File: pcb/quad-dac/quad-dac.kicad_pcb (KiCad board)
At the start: 2 copper layers, 90 x 90 mm, 18 parts, among them J1 Power+SPI, J2 CV_OUT, U1 AD5754R

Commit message: pcbs
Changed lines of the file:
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@@
   ;; =========================================================================
   ;; ── U1: AD5754R — TSSOP-24 ────────────────────────────────────────────
+  ;; Pin mapping: AD5754R pin 1 (AVSS) at top-left → KiCad pad 1 at (-2.8625, 3.575)
+  ;; Counter-clockwise: pads 1-12 left side (top→bottom), pads 13-24 right side (bottom→top)
   (footprint "Package_SO:TSSOP-24_4.4x7.8mm_P0.65mm"
     (layer "F.Cu")
@@
     (property "Value" "AD5754R" (at 45 52 0) (layer "F.Fab")
       (effects (font (size 1.0 1.0) (thickness 0.15))))
-    (pad "1" smd rect (at -6.175 -5.85 0) (size 1.5 0.35) (layers "F.Cu" "F.Paste" "F.Mask") (net 2))
-    (pad "2" smd rect (at -6.175 -5.2 0) (size 1.5 0.35) (layers "F.Cu" "F.Paste" "F.Mask") (net 4))
-    (pad "3" smd rect (at -6.175 -4.55 0) (size 1.5 0.35) (layers "F.Cu" "F.Paste" "F.Mask") (net 9))
-    (pad "4" smd rect (at -6.175 -3.9 0) (size 1.5 0.35) (layers "F.Cu" "F.Paste" "F.Mask") (net 10))
-    (pad "5" smd rect (at -6.175 -3.25 0) (size 1.5 0.35) (layers "F.Cu" "F.Paste" "F.Mask") (net 0))
-    (pad "6" smd rect (at -6.175 -2.6 0) (size 1.5 0.35) (layers "F.Cu" "F.Paste" "F.Mask") (net 0))
-    (pad "7" smd rect (at -6.175 -1.95 0) (size 1.5 0.35) (layers "F.Cu" "F.Paste" "F.Mask") (net 0))
-    (pad "8" smd rect (at -6.175 -1.3 0) (size 1.5 0.35) (layers "F.Cu" "F.Paste" "F.Mask") (net 11))
-    (pad "9" smd rect (at -6.175 -0.65 0) (size 1.5 0.35) (layers "F.Cu" "F.Paste" "F.Mask") (net 12))
-    (pad "10" smd rect (at -6.175 0.0 0) (size 1.5 0.35) (layers "F.Cu" "F.Paste" "F.Mask") (net 4))
-    (pad "11" smd rect (at -6.175 0.65 0) (size 1.5 0.35) (layers "F.Cu" "F.Paste" "F.Mask") (net 4))
-    (pad "12" smd rect (at 6.175 0.65 0) (size 1.5 0.35) (layers "F.Cu" "F.Paste" "F.Mask") (net 3))
-    (pad "13" smd rect (at 6.175 0.0 0) (size 1.5 0.35) (layers "F.Cu" "F.Paste" "F.Mask") (net 4))
-    (pad "14" smd rect (at 6.175 -0.65 0) (size 1.5 0.35) (layers "F.Cu" "F.Paste" "F.Mask") (net 6))
-    (pad "15" smd rect (at 6.175 -1.3 0) (size 1.5 0.35) (layers "F.Cu" "F.Paste" "F.Mask") (net 7))
-    (pad "16" smd rect (at 6.175 -1.95 0) (size 1.5 0.35) (layers "F.Cu" "F.Paste" "F.Mask") (net 5))
-    (pad "17" smd rect (at 6.175 -2.6 0) (size 1.5 0.35) (layers "F.Cu" "F.Paste" "F.Mask") (net 8))
-    (pad "18" smd rect (at 6.175 -3.25 0) (size 1.5 0.35) (layers "F.Cu" "F.Paste" "F.Mask") (net 4))
-    (pad "19" smd rect (at 6.175 -3.9 0) (size 1.5 0.35) (layers "F.Cu" "F.Paste" "F.Mask") (net 14))
-    (pad "20" smd rect (at 6.175 -4.55 0) (size 1.5 0.35) (layers "F.Cu" "F.Paste" "F.Mask") (net 0))
-    (pad "21" smd rect (at 6.175 -5.2 0) (size 1.5 0.35) (layers "F.Cu" "F.Paste" "F.Mask") (net 4))
-    (pad "22" smd rect (at 6.175 -5.85 0) (size 1.5 0.35) (layers "F.Cu" "F.Paste" "F.Mask") (net 13))
-    (pad "23" smd rect (at -6.175 0.65 0) (size 1.5 0.35) (layers "F.Cu" "F.Paste" "F.Mask") (net 4))
-    (pad "24" smd rect (at -6.175 5.85 0) (size 1.5 0.35) (layers "F.Cu" "F.Paste" "F.Mask") (net 1))
+    (pad "1" smd roundrect (at -2.8625 3.575) (size 1.475 0.4) (layers "F.Cu" "F.Paste" "F.Mask") (net 2) (roundrect_rratio 0.25))
+    (pad "2" smd roundrect (at -2.8625 2.925) (size 1.475 0.4) (layers "F.Cu" "F.Paste" "F.Mask") (net 4) (roundrect_rratio 0.25))
+    (pad "3" smd roundrect (at -2.8625 2.275) (size 1.475 0.4) (layers "F.Cu" "F.Paste" "F.Mask") (net 9) (roundrect_rratio 0.25))
+    (pad "4" smd roundrect (at -2.8625 1.625) (size 1.475 0.4) (layers "F.Cu" "F.Paste" "F.Mask") (net 10) (roundrect_rratio 0.25))
+    (pad "5" smd roundrect (at -2.8625 0.975) (size 1.475 0.4) (layers "F.Cu" "F.Paste" "F.Mask") (net 0) (roundrect_rratio 0.25))
+    (pad "6" smd roundrect (at -2.8625 0.325) (size 1.475 0.4) (layers "F.Cu" "F.Paste" "F.Mask") (net 0) (roundrect_rratio 0.25))
+    (pad "7" smd roundrect (at -2.8625 -0.325) (size 1.475 0.4) (layers "F.Cu" "F.Paste" "F.Mask") (net 0) (roundrect_rratio 0.25))
+    (pad "8" smd roundrect (at -2.8625 -0.975) (size 1.475 0.4) (layers "F.Cu" "F.Paste" "F.Mask") (net 11) (roundrect_rratio 0.25))
+    (pad "9" smd roundrect (at -2.8625 -1.625) (size 1.475 0.4) (layers "F.Cu" "F.Paste" "F.Mask") (net 12) (roundrect_rratio 0.25))
+    (pad "10" smd roundrect (at -2.8625 -2.275) (size 1.475 0.4) (layers "F.Cu" "F.Paste" "F.Mask") (net 4) (roundrect_rratio 0.25))
+    (pad "11" smd roundrect (at -2.8625 -2.925) (size 1.475 0.4) (layers "F.Cu" "F.Paste" "F.Mask") (net 4) (roundrect_rratio 0.25))
+    (pad "12" smd roundrect (at -2.8625 -3.575) (size 1.475 0.4) (layers "F.Cu" "F.Paste" "F.Mask") (net 3) (roundrect_rratio 0.25))
+    (pad "13" smd roundrect (at 2.8625 -3.575) (size 1.475 0.4) (layers "F.Cu" "F.Paste" "F.Mask") (net 4) (roundrect_rratio 0.25))
+    (pad "14" smd roundrect (at 2.8625 -2.925) (size 1.475 0.4) (layers "F.Cu" "F.Paste" "F.Mask") (net 6) (roundrect_rratio 0.25))
+    (pad "15" smd roundrect (at 2.8625 -2.275) (size 1.475 0.4) (layers "F.Cu" "F.Paste" "F.Mask") (net 7) (roundrect_rratio 0.25))
+    (pad "16" smd roundrect (at 2.8625 -1.625) (size 1.475 0.4) (layers "F.Cu" "F.Paste" "F.Mask") (net 5) (roundrect_rratio 0.25))
+    (pad "17" smd roundrect (at 2.8625 -0.975) (size 1.475 0.4) (layers "F.Cu" "F.Paste" "F.Mask") (net 8) (roundrect_rratio 0.25))
+    (pad "18" smd roundrect (at 2.8625 -0.325) (size 1.475 0.4) (layers "F.Cu" "F.Paste" "F.Mask") (net 4) (roundrect_rratio 0.25))
+    (pad "19" smd roundrect (at 2.8625 0.325) (size 1.475 0.4) (layers "F.Cu" "F.Paste" "F.Mask") (net 14) (roundrect_rratio 0.25))
+    (pad "20" smd roundrect (at 2.8625 0.975) (size 1.475 0.4) (layers "F.Cu" "F.Paste" "F.Mask") (net 0) (roundrect_rratio 0.25))
+    (pad "21" smd roundrect (at 2.8625 1.625) (size 1.475 0.4) (layers "F.Cu" "F.Paste" "F.Mask") (net 4) (roundrect_rratio 0.25))
+    (pad "22" smd roundrect (at 2.8625 2.275) (size 1.475 0.4) (layers "F.Cu" "F.Paste" "F.Mask") (net 13) (roundrect_rratio 0.25))
+    (pad "23" smd roundrect (at 2.8625 2.925) (size 1.475 0.4) (layers "F.Cu" "F.Paste" "F.Mask") (net 4) (roundrect_rratio 0.25))
+    (pad "24" smd roundrect (at 2.8625 3.575) (size 1.475 0.4) (layers "F.Cu" "F.Paste" "F.Mask") (net 1) (roundrect_rratio 0.25))
   )
   ;; ── J1: 2x5 Power+SPI Header ──────────────────────────────────────────

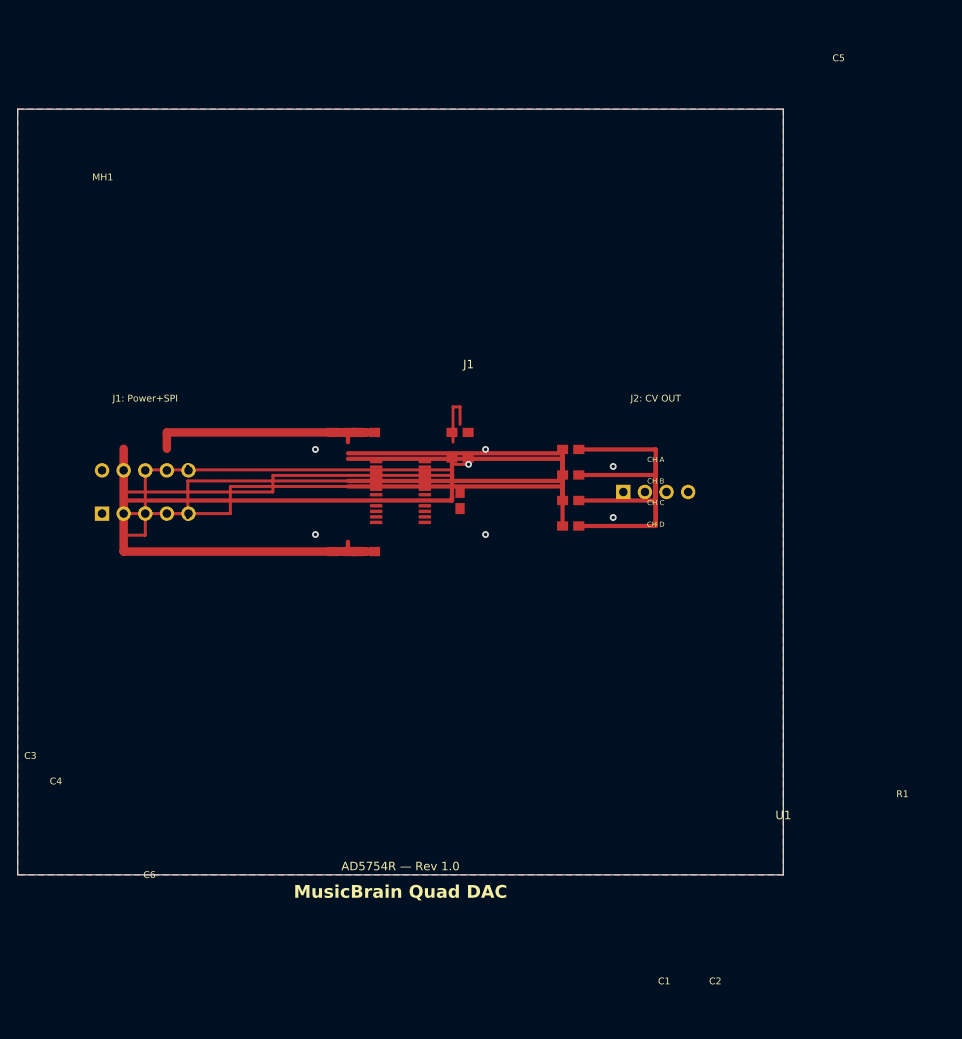
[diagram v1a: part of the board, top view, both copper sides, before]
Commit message: save patch via CC#102 >63 en terug (tot 64 patches vol zijn)
What I changed

Persistent patch bank in firmware
Added LittleFS-backed bank storage in main.cpp:260.
Bank file: patchbank.bin in Teensy program flash.
128 slots, each storing:
full Elements Patch struct
performance modulation (CC30 result)
reverb amount/time
MIDI controls for MVP
Save trigger CC:
CC 102, value >= 64 saves current patch to next slot
edge-triggered (must go below 64 before next save)
logic at main.cpp:491
Program Change recall:
Program 0..127 recalls slot 0..127 (if present)
handler hookup at main.cpp:652
Boot/load behavior
LittleFS init + bank load/restore at startup in main.cpp:398 and main.cpp:628
Boot message with controls at main.cpp:657
Version + docs
Firmware version bumped to 0.5.5 in FwVersion.h:4
MIDI and MVP docs updated in README.md:75
Version history updated in README.md:107
Architecture version history updated in architecture.md:828
Build and upload status

Build: SUCCESS.
Upload command completed, but your COM5 was busy and Teensy requested manual program button:
message indicated Access is denied on COM5 and asked to press PROGRAM MODE button.
So firmware is built and ready; if needed, press Teensy program button once and rerun upload (or close anything holding COM5 first).
How to use from MIDI-OX right now

Save current patch to next slot:
send B0 66 7F
then send B0 66 00 to re-arm trigger
Recall patch slot N:
send C0 NN (NN = 00..7F)
Notes

This now survives reboot and firmware updates because bank data is in LittleFS program flash.
If no bank exists yet, firmware creates an empty one on first boot.
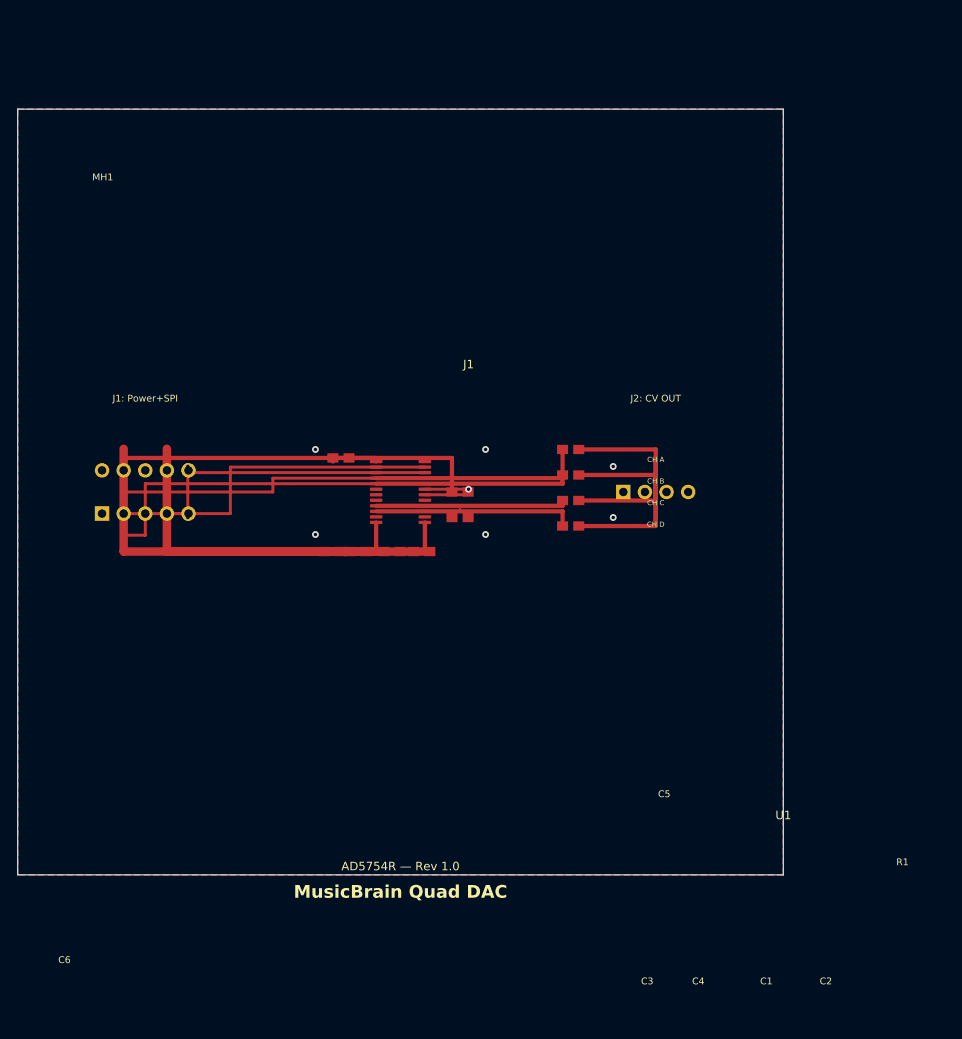
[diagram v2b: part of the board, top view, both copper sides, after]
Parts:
- moved C5 14.9 mm to (38.0, 41.0), turned to 0 degrees
- moved C3 14.0 mm to (37.0, 52.0), turned to 0 degrees
- moved C4 14.0 mm to (40.0, 52.0), turned to 0 degrees
- moved C6 10.0 mm to (52.0, 48.0)
- moved C2 6.50 mm to (47.5, 52.0)
- moved C1 6.00 mm to (44.0, 52.0)
- moved R1 4.00 mm to (52.0, 45.0)
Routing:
- net -12V: track 28.7 -> 40.1 mm
- net VOUT_A: track 50.6 -> 40.5 mm
- net VOUT_B: track 41.4 -> 33.9 mm
- net +12V: track 43.9 -> 50.9 mm
- net CS: track 46.4 -> 41.5 mm
- net VOUT_D: track 47.4 -> 43.1 mm
- net MOSI: track 40.7 -> 37.0 mm
- net Net-(U1-CLR): track 1.88 -> 5.41 mm
- net GND: track 1.83 -> 5.14 mm
- net VOUT_C: track 38.2 -> 35.3 mm
- net Net-(U1-REFIN): track 7.02 -> 4.36 mm
- net +3V3: track 47.6 -> 50.0 mm
- net MISO: track 37.5 -> 35.1 mm
- net SCK: track 41.9 -> 40.9 mm
